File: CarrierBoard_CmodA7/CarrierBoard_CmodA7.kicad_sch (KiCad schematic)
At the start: 62 parts

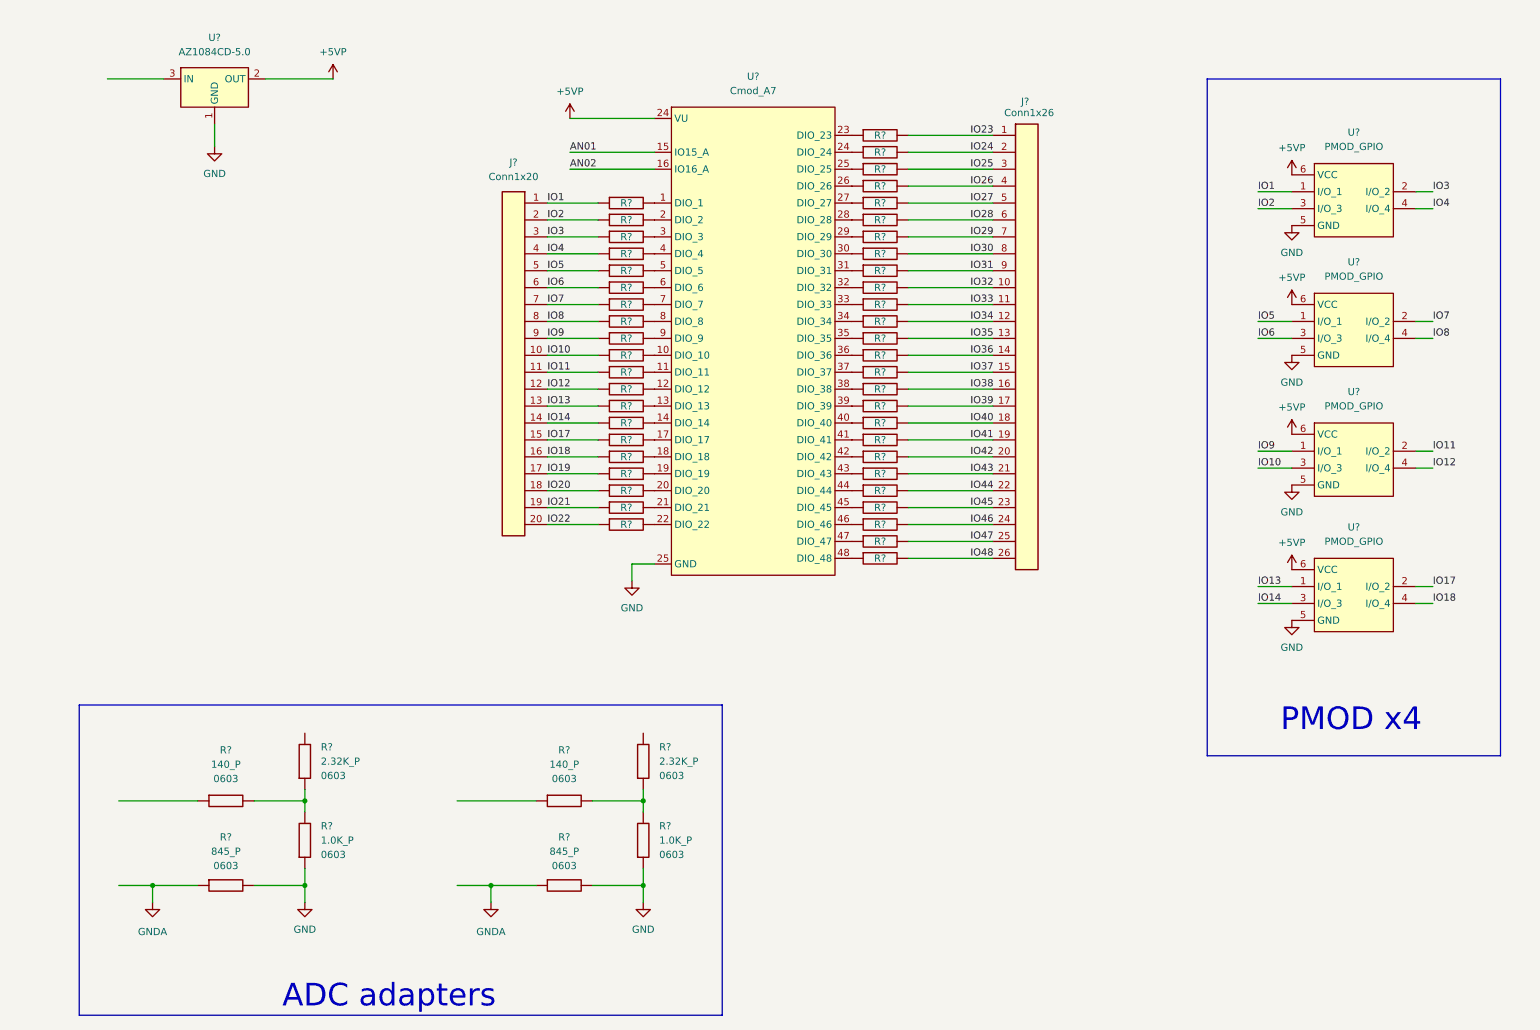
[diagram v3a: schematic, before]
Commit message: añadido condensadores power supply
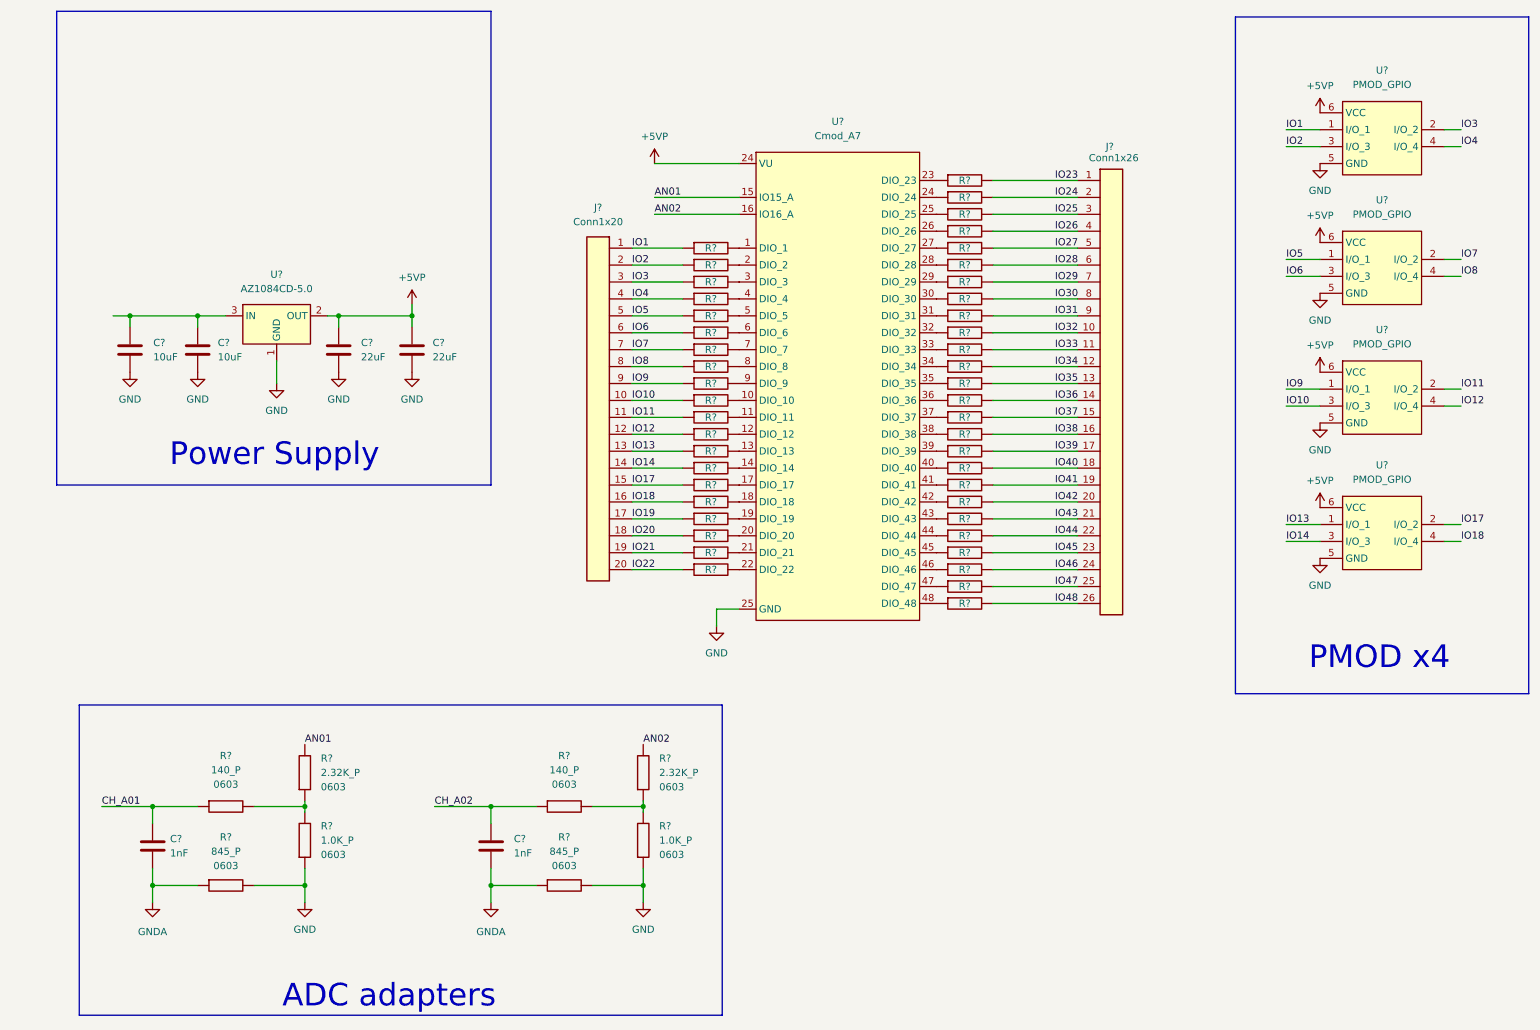
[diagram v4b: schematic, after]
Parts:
- added C? (x2): 22uF, Capacitor_SMD:C_0805_2012Metric, symbol Herranz - Capacitor (0805):Gen_C
- added C? (x2): 10uF, Capacitor_SMD:C_0805_2012Metric, symbol Herranz - Capacitor (0805):Gen_C
- added C? (x2): 1nF, Capacitor_SMD:C_0603_1608Metric, symbol Herranz - Capacitor (0603):Gen_C
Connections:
- net +5VP: now also C?.1, C?.1
- net AN01: now also R?.2
- net AN02: now also R?.2
- net GND: now also C?.2, C?.2, C?.2, C?.2
- net GNDA: now also C?.2, C?.2
- net at U?.3 (IN): now also C?.1, C?.1
- net CH_A01: now reaches R?.1
- net CH_A01: now also C?.1
- net CH_A02: now reaches R?.1
- net CH_A02: now also C?.1
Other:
- note added: "Power Supply"
- title: (none) -> C-Mod A7 Carrier Board
- moved on the sheet: J?, R?, U?

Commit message: Arreglado el circuto del ADC
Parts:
- removed C?: 22uF, Capacitor_SMD:C_0805_2012Metric, symbol Herranz - Capacitor (0805):Gen_C
- removed C?: 10uF, Capacitor_SMD:C_0805_2012Metric, symbol Herranz - Capacitor (0805):Gen_C
- removed J?: Conn1x20, Connector_PinHeader_2.54mm:PinHeader_1x20_P2.54mm_Vertical, symbol Herranz - Gen Connectors:Conn1x20
- removed R? (x2): 1.0K, Resistor_SMD:R_0603_1608Metric, symbol Herranz - Resistors (0603):1.0K
- added C2: 22uF, Capacitor_SMD:C_0805_2012Metric, symbol Herranz - Capacitor (0805):Gen_C
- added C3: 10uF, Capacitor_SMD:C_0805_2012Metric, symbol Herranz - Capacitor (0805):Gen_C
- added CN1: Mini-Fit_Jr._Header,_2_Circuits, Herranz - Conn Molex:Mini-Fit Jr. Header, 2 Circuits, symbol Herranz - Conn Molex:Mini-Fit_Jr._Header,_2_Circuits
- added LD1: LED_Generic, LED_SMD:LED_0603_1608Metric_Pad1.05x0.95mm_HandSolder, symbol Herranz - HighpowerLED:LED_Generic
- added R47: 1.0K, Resistor_SMD:R_0603_1608Metric, symbol Herranz - Resistors (0603):1.0K
- added U7: Conn1x21, Connector_PinSocket_2.54mm:PinSocket_1x22_P2.54mm_Vertical, symbol Herranz - Gen Connectors:Conn1x21
- J2: renamed from J?; footprint Connector_PinHeader_2.54mm:PinHeader_1x26_P2.54mm_Vertical -> Connector_PinSocket_2.54mm:PinSocket_1x26_P2.54mm_Vertical
- U2: renamed from U?; footprint (none) -> Herranz - DevBoards:CmodA7
- U3, U4, U5, U6: renamed from U?; footprint Connector_PinHeader_2.54mm:PinHeader_2x03_P2.54mm_Horizontal -> Connector_PinSocket_2.54mm:PinSocket_2x03_P2.54mm_Horizontal
- gave numbers to parts that had none: 57
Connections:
- net GNDA is gone; now on net GND: C5.2, C6.2, R49.1, R53.1
- net IO24 is gone; now on net AN01: J2.2 (Pin_2)
- net IO25 is gone; now on net GND: J2.3 (Pin_3)
- net +5VP: now also C3.1, R47.2
- net AN01: now also C5.1, R48.1; no longer R50.2, U2.15 (IO15_A)
- net AN02: now also C6.1, J2.1 (Pin_1), R52.1; no longer R54.2, U2.16 (IO16_A)
- net CH_A01: now also R50.2, U2.15 (IO15_A); no longer C5.1, R48.1
- net CH_A02: now also R54.2, U2.16 (IO16_A); no longer C6.1, R52.1
- net GND: now also C2.2, C3.2, CN1.2, LD1.2 (K)
- net IO1: now also U3.3 (I/O_3), U7.1 (Pin_1); no longer U3.1 (I/O_1)
- net IO10: now also U5.4 (I/O_4), U7.10 (Pin_10); no longer U5.3 (I/O_3)
- net IO11: now also U5.1 (I/O_1), U7.11 (Pin_11); no longer U5.2 (I/O_2)
- net IO12: now also U5.2 (I/O_2), U7.12 (Pin_12); no longer U5.4 (I/O_4)
- net IO13: now also U6.3 (I/O_3), U7.13 (Pin_13); no longer U6.1 (I/O_1)
- net IO14: now also U6.4 (I/O_4), U7.14 (Pin_14); no longer U6.3 (I/O_3)
- net IO17: now also U6.1 (I/O_1), U7.15 (Pin_15); no longer U6.2 (I/O_2)
- net IO18: now also U6.2 (I/O_2), U7.16 (Pin_16); no longer U6.4 (I/O_4)
- net IO19: now also U7.17 (Pin_17)
- net IO2: now also U3.4 (I/O_4), U7.2 (Pin_2); no longer U3.3 (I/O_3)
- net IO20: now also U7.18 (Pin_18)
- net IO21: now also U7.19 (Pin_19)
- net IO22: now also U7.20 (Pin_20)
- net IO23: now also R21.1, U7.21 (Pin_21); no longer J2.1 (Pin_1), R21.2
- net IO3: now also U3.1 (I/O_1), U7.3 (Pin_3); no longer U3.2 (I/O_2)
- net IO4: now also U3.2 (I/O_2), U7.4 (Pin_4); no longer U3.4 (I/O_4)
- net IO5: now also U4.3 (I/O_3), U7.5 (Pin_5); no longer U4.1 (I/O_1)
- net IO6: now also U4.4 (I/O_4), U7.6 (Pin_6); no longer U4.3 (I/O_3)
- net IO7: now also U4.1 (I/O_1), U7.7 (Pin_7); no longer U4.2 (I/O_2)
- net IO8: now also U4.2 (I/O_2), U7.8 (Pin_8); no longer U4.4 (I/O_4)
- net IO9: now also U5.3 (I/O_3), U7.9 (Pin_9); no longer U5.1 (I/O_1)
- net at C1.1, U1.3 (IN): now also C2.1, CN1.1
- net at U2.23 (DIO_23): now also R21.2; no longer R21.1
- new net: LD1.1 (A), R47.1
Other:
- moved on the sheet: C1, C4, C5, C6, J2, R1, R10, R11, R12, R13, R14, R15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

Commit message: Arreglado Tira pines 1x22 a 1x21, cambiado el nivel de prioridad de los planos de cobre
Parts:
- U7: footprint Connector_PinSocket_2.54mm:PinSocket_1x22_P2.54mm_Vertical -> Connector_PinSocket_2.54mm:PinSocket_1x21_P2.54mm_Vertical
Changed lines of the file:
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@@
     (property "Reference" "U7" (id 0) (at 48 105.41 0))
     (property "Value" "Conn1x21" (id 1) (at 48 107.95 0))
-    (property "Footprint" "Connector_PinSocket_2.54mm:PinSocket_1x22_P2.54mm_Vertical" (id 2) (at 48 176 0)
+    (property "Footprint" "Connector_PinSocket_2.54mm:PinSocket_1x21_P2.54mm_Vertical" (id 2) (at 48 176 0)
       (effects (font (size 1.27 1.27)) hide)
     )
@@
     )
     (path "/2a3df55c-3473-4122-8bb3-c4a2678251ae"
-      (reference "U7") (unit 1) (value "Conn1x21") (footprint "Connector_PinSocket_2.54mm:PinSocket_1x22_P2.54mm_Vertical")
-    )
-  )
+      (reference "U7") (unit 1) (value "Conn1x21") (footprint "Connector_PinSocket_2.54mm:PinSocket_1x21_P2.54mm_Vertical")
+    )
+  )

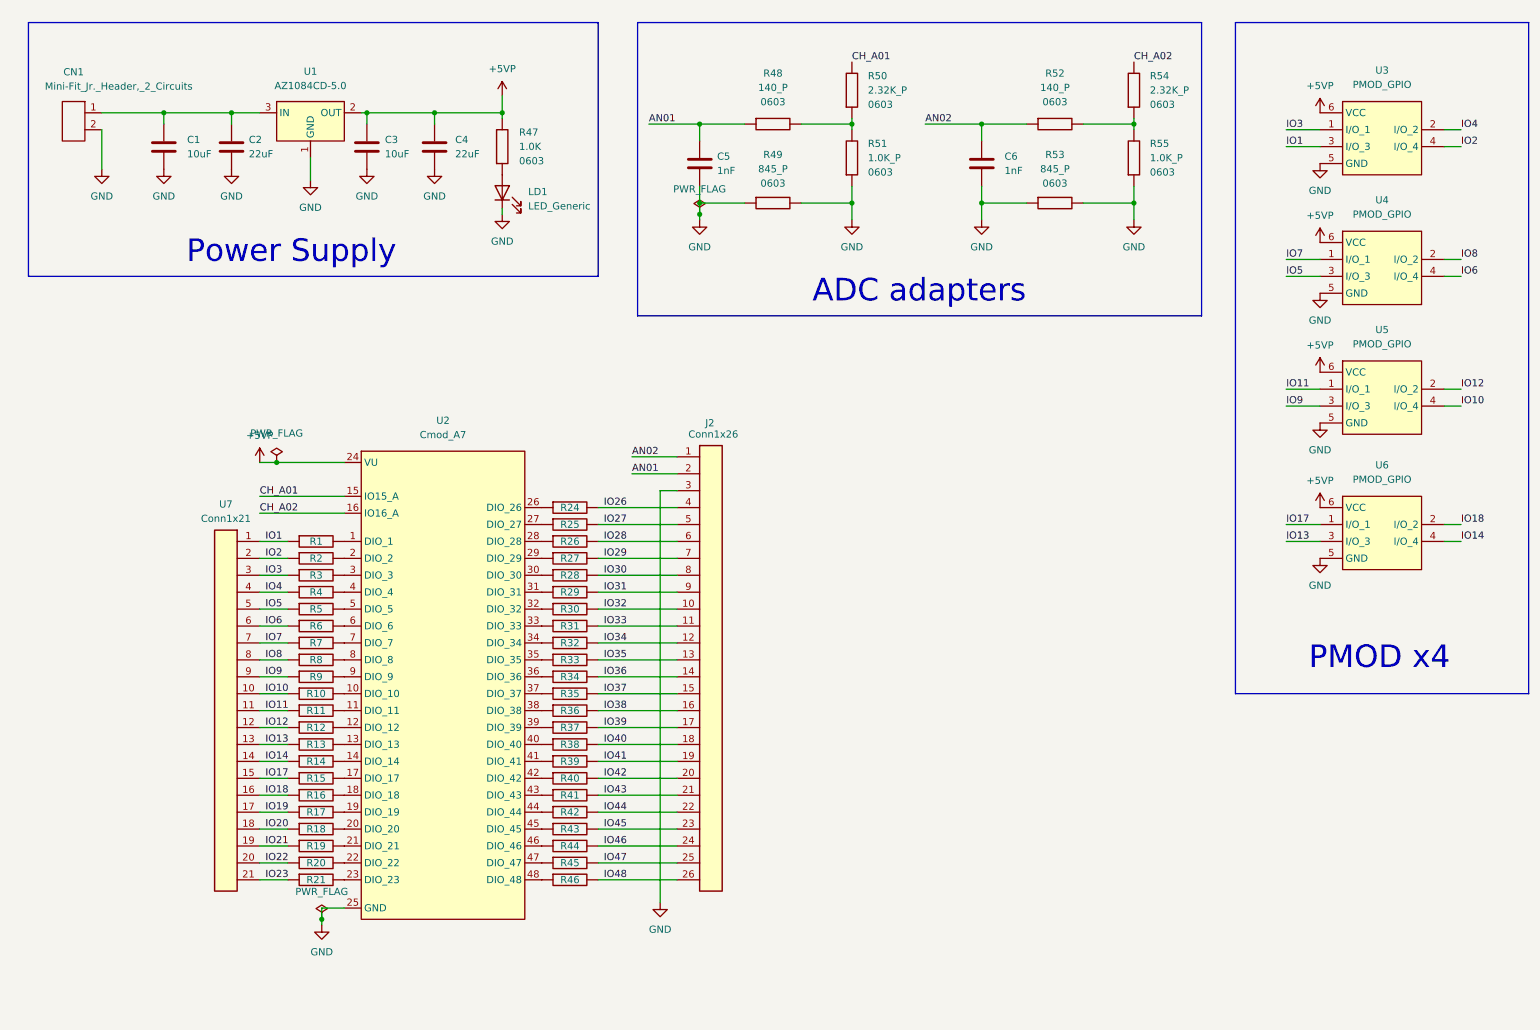
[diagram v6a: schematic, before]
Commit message: arreglado divisor de tension y filtro del ADC.
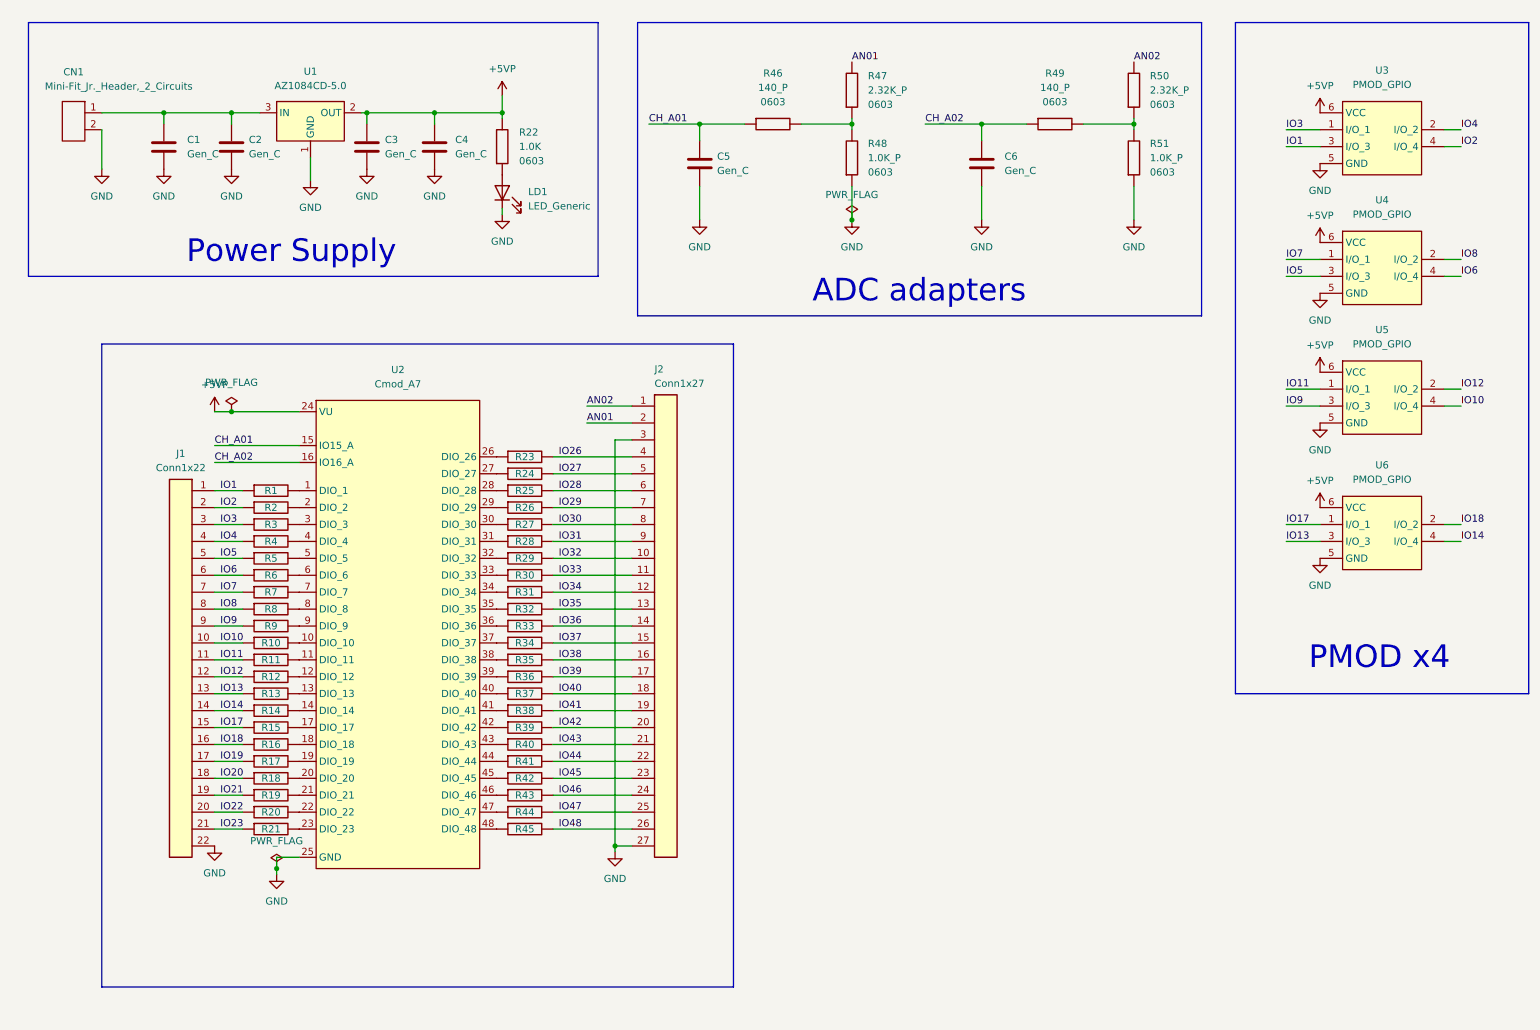
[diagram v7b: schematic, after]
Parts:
- removed J2: Conn1x26, Connector_PinSocket_2.54mm:PinSocket_1x26_P2.54mm_Vertical, symbol Herranz - Gen Connectors:Conn1x26
- removed R49, R53: 845_P, Resistor_SMD:R_0603_1608Metric, symbol Herranz - Resistors (0603):845_P
- removed U7: Conn1x21, Connector_PinSocket_2.54mm:PinSocket_1x21_P2.54mm_Vertical, symbol Herranz - Gen Connectors:Conn1x21
- added J1: Conn1x22, Connector_PinSocket_2.54mm:PinSocket_1x22_P2.54mm_Vertical, symbol Herranz - Gen Connectors:Conn1x22
- added J2: Conn1x27, Connector_PinSocket_2.54mm:PinSocket_1x27_P2.54mm_Vertical, symbol Herranz - Gen Connectors:Conn1x27
- C1, C3: value 10uF -> Gen_C
- C2, C4: value 22uF -> Gen_C
- C5, C6: value 1nF -> Gen_C
- renumbered R47 to R22, R24 to R23, R25 to R24, R26 to R25, R27 to R26, R28 to R27, R29 to R28, R30 to R29, R31 to R30, R32 to R31, R33 to R32, R34 to R33, R35 to R34, R36 to R35, R37 to R36, R38 to R37, R39 to R38, R40 to R39, R41 to R40, R42 to R41, R43 to R42, R44 to R43, R45 to R44, R46 to R45, R48 to R46, R50 to R47, R51 to R48, R52 to R49, R54 to R50, R55 to R51
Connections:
- net AN01: now also R47.2, J2.2 (Pin_2); no longer C5.1, R46.1
- net AN02: now also R50.2, J2.1 (Pin_1); no longer C6.1, R49.1
- net CH_A01: now also C5.1, R46.1; no longer R47.2
- net CH_A02: now also C6.1, R49.1; no longer R50.2
- net GND: now also J1.22 (Pin_22), J2.27 (Pin_27), J2.3 (Pin_3)
- net IO1: now also J1.1 (Pin_1)
- net IO10: now also J1.10 (Pin_10)
- net IO11: now also J1.11 (Pin_11)
- net IO12: now also J1.12 (Pin_12)
- net IO13: now also J1.13 (Pin_13)
- net IO14: now also J1.14 (Pin_14)
- net IO17: now also J1.15 (Pin_15)
- net IO18: now also J1.16 (Pin_16)
- net IO19: now also J1.17 (Pin_17)
- net IO2: now also J1.2 (Pin_2)
- net IO20: now also J1.18 (Pin_18)
- net IO21: now also J1.19 (Pin_19)
- net IO22: now also J1.20 (Pin_20)
- net IO23: now also J1.21 (Pin_21)
- net IO26: now also J2.4 (Pin_4)
- net IO27: now also J2.5 (Pin_5)
- net IO28: now also J2.6 (Pin_6)
- net IO29: now also J2.7 (Pin_7)
- net IO3: now also J1.3 (Pin_3)
- net IO30: now also J2.8 (Pin_8)
- net IO31: now also J2.9 (Pin_9)
- net IO32: now also J2.10 (Pin_10)
- net IO33: now also J2.11 (Pin_11)
- net IO34: now also J2.12 (Pin_12)
- net IO35: now also J2.13 (Pin_13)
- net IO36: now also J2.14 (Pin_14)
- net IO37: now also J2.15 (Pin_15)
- net IO38: now also J2.16 (Pin_16)
- net IO39: now also J2.17 (Pin_17)
- net IO4: now also J1.4 (Pin_4)
- net IO40: now also J2.18 (Pin_18)
- net IO41: now also J2.19 (Pin_19)
- net IO42: now also J2.20 (Pin_20)
- net IO43: now also J2.21 (Pin_21)
- net IO44: now also J2.22 (Pin_22)
- net IO45: now also J2.23 (Pin_23)
- net IO46: now also J2.24 (Pin_24)
- net IO47: now also J2.25 (Pin_25)
- net IO48: now also J2.26 (Pin_26)
- net IO5: now also J1.5 (Pin_5)
- net IO6: now also J1.6 (Pin_6)
- net IO7: now also J1.7 (Pin_7)
- net IO8: now also J1.8 (Pin_8)
- net IO9: now also J1.9 (Pin_9)
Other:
- moved on the sheet: R1, R10, R11, R12, R13, R14, R15, R16, R17, R18, R19, R2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
